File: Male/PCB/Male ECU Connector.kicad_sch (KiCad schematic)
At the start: 5 parts, among them J1 ANALYZER, J2 ECU, J3 DJetECUEdgeConnector, K1 G5V-1-DC5

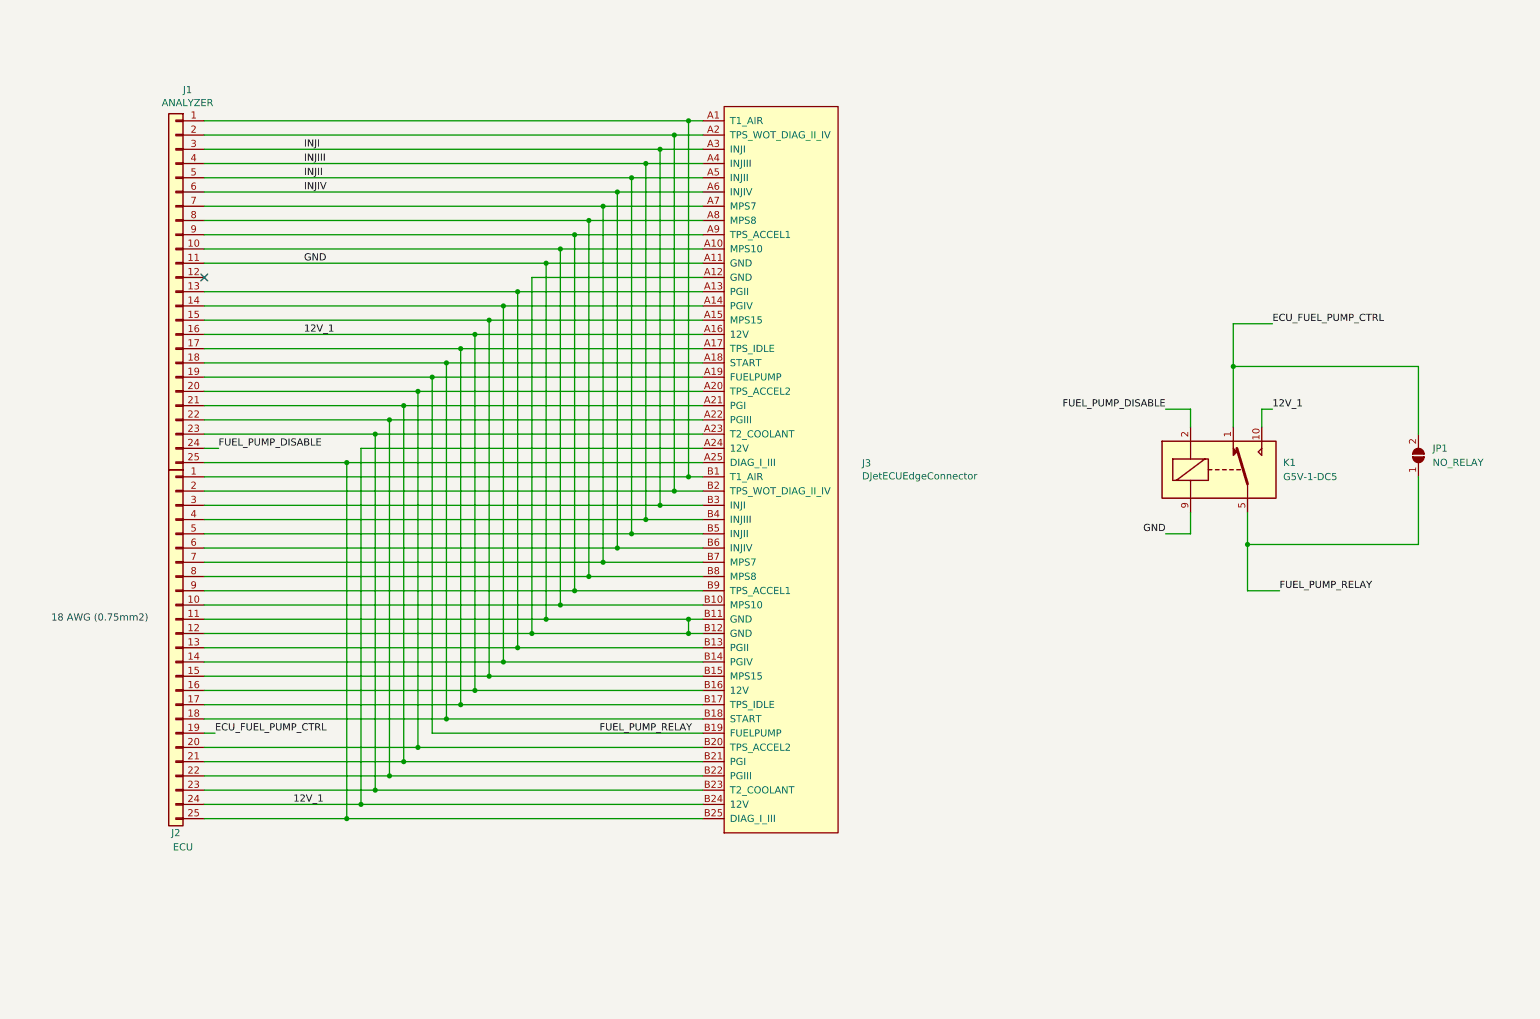
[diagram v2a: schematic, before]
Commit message: Laid out PCB fpr male connector.
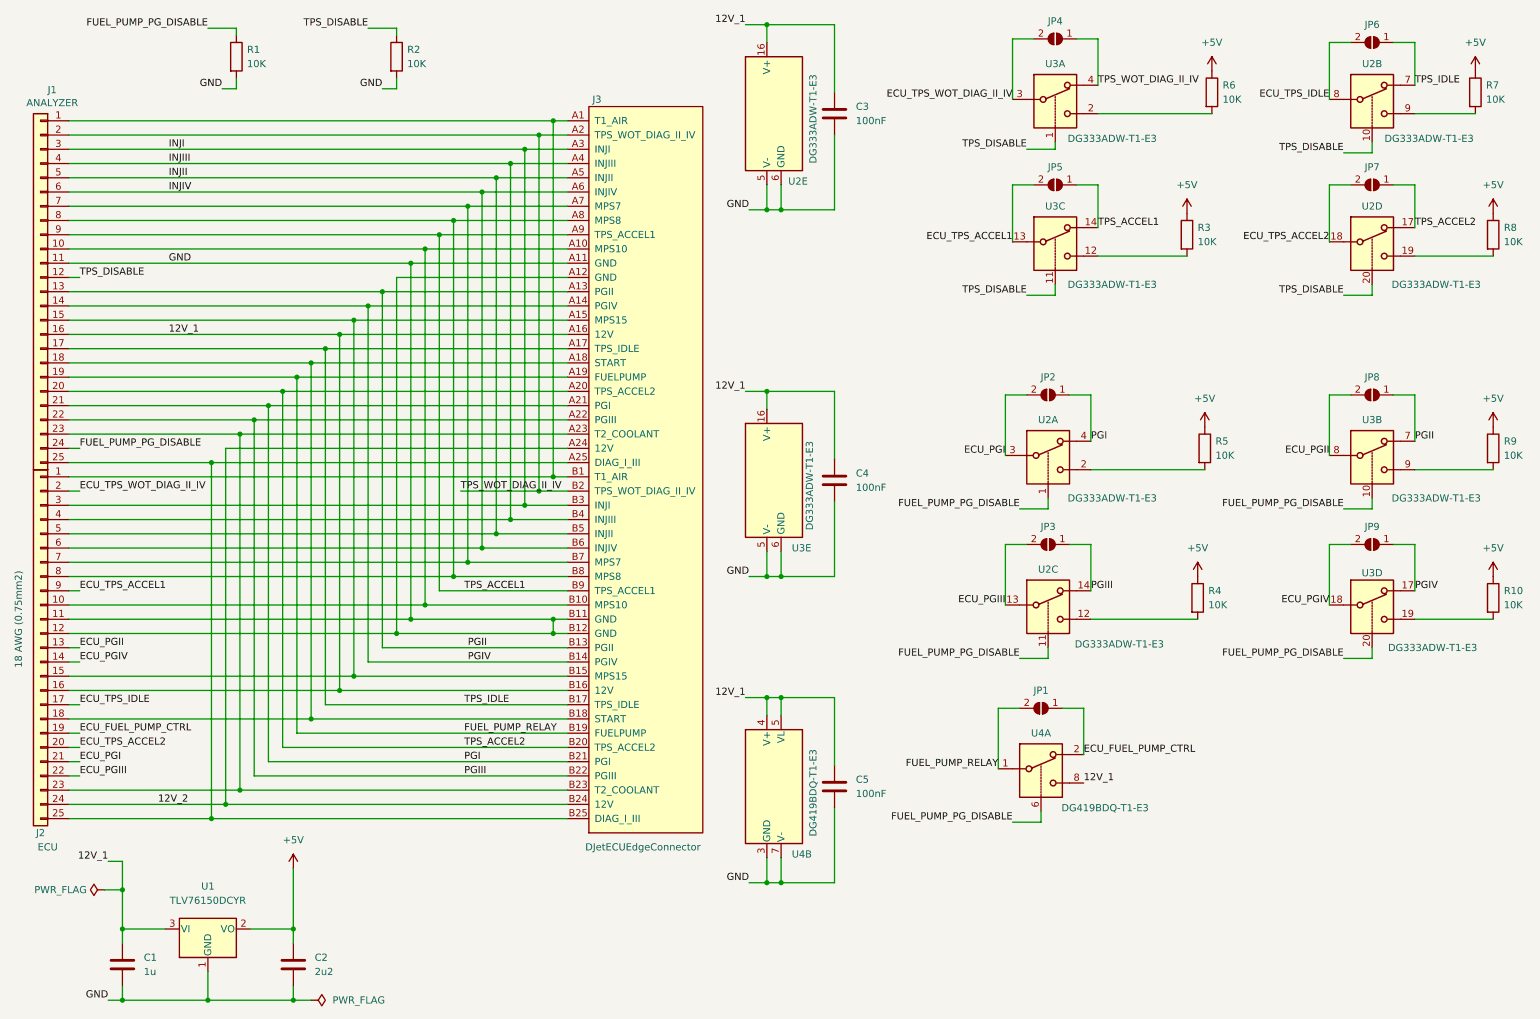
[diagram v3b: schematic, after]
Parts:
- removed K1: G5V-1-DC5, Relay_THT:Relay_SPDT_Omron_G5V-1, symbol Relay:G5V-1
- added C1: 1u, Capacitor_SMD:C_0603_1608Metric, symbol Device:C
- added C2: 2u2, Capacitor_SMD:C_0603_1608Metric, symbol Device:C
- added C3, C4, C5: 100nF, Capacitor_SMD:C_0603_1608Metric, symbol Device:C
- added JP2, JP3, JP4, JP5, JP6, JP7, JP8, JP9: NO_ANALYZER, Jumper:SolderJumper-2_P1.3mm_Open_TrianglePad1.0x1.5mm, symbol Jumper:SolderJumper_2_Open
- added R1, R10, R2, R3, R4, R5, R6, R7, R8, R9: 10K, Resistor_SMD:R_0603_1608Metric, symbol Device:R
- added U1: TLV76150DCYR, Package_TO_SOT_SMD:SOT-223-3_TabPin2, symbol Regulator_Linear:LM1117-5.0
- added U2, U3: DG333ADW-T1-E3, Package_SO:SOIC-20W_7.5x12.8mm_P1.27mm, symbol Analog_Switch:MAX333A
- added U4: DG419BDQ-T1-E3, Package_SO:MSOP-8_3x3mm_P0.65mm, symbol Analog_Switch:DG419xY
- JP1: value NO_RELAY -> NO_ANALYZER
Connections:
- net 12V_1: now also C1.1, C3.1, C4.1, C5.1, U1.3 (VI), U2.16 (V+), U3.16 (V+), U4.4 (V+), U4.5 (VL), U4.8; no longer J2.24 (Pin_24), J3.A24 (12V), J3.B24 (12V)
- net ECU_FUEL_PUMP_CTRL: now also JP1.1 (A), U4.2; no longer JP1.2 (B)
- net FUEL_PUMP_RELAY: now also JP1.2 (B), U4.1; no longer JP1.1 (A)
- net GND: now also C1.2, C2.2, C3.2, C4.2, C5.2, R1.2, R2.2, U1.1 (GND), U2.5 (V-), U2.6 (GND), U3.5 (V-), U3.6 (GND), U4.3 (GND), U4.7 (V-)
- net TPS_DISABLE: now reaches J1.12 (Pin_12)
- net TPS_DISABLE: now also R2.1, U2.10, U2.20, U3.1, U3.11
- net PGII: now reaches J1.13 (Pin_13), J3.A13 (PGII), J3.B13 (PGII)
- net PGII: now also JP8.1 (A), U3.7; no longer J2.13 (Pin_13)
- net PGIV: now reaches J1.14 (Pin_14), J3.A14 (PGIV), J3.B14 (PGIV)
- net PGIV: now also JP9.1 (A), U3.17; no longer J2.14 (Pin_14)
- net TPS_IDLE: now reaches J1.17 (Pin_17), J3.A17 (TPS_IDLE), J3.B17 (TPS_IDLE)
- net TPS_IDLE: now also JP6.1 (A), U2.7; no longer J2.17 (Pin_17)
- net TPS_WOT_DIAG_II_IV: now reaches J1.2 (Pin_2), J3.A2 (TPS_WOT_DIAG_II_IV), J3.B2 (TPS_WOT_DIAG_II_IV)
- net TPS_WOT_DIAG_II_IV: now also JP4.1 (A), U3.4; no longer J2.2 (Pin_2)
- net TPS_ACCEL2: now reaches J1.20 (Pin_20), J3.A20 (TPS_ACCEL2), J3.B20 (TPS_ACCEL2)
- net TPS_ACCEL2: now also JP7.1 (A), U2.17; no longer J2.20 (Pin_20)
- net PGI: now reaches J1.21 (Pin_21), J3.A21 (PGI), J3.B21 (PGI)
- net PGI: now also JP2.1 (A), U2.4; no longer J2.21 (Pin_21)
- net PGIII: now reaches J1.22 (Pin_22), J3.A22 (PGIII), J3.B22 (PGIII)
- net PGIII: now also JP3.1 (A), U2.14; no longer J2.22 (Pin_22)
- net TPS_ACCEL1: now reaches J1.9 (Pin_9), J3.A9 (TPS_ACCEL1), J3.B9 (TPS_ACCEL1)
- net TPS_ACCEL1: now also JP5.1 (A), U3.14; no longer J2.9 (Pin_9)
- net FUEL_PUMP_DISABLE renamed FUEL_PUMP_PG_DISABLE
- net FUEL_PUMP_PG_DISABLE: now also R1.1, U2.1, U2.11, U3.10, U3.20, U4.6
- new net: R5.2, U2.2
- new net: R3.2, U3.12
- new net: R10.2, U3.19
- new net: R9.2, U3.9
- new net: R6.2, U3.2
- new net: R8.2, U2.19
- new net: R4.2, U2.12
- new net: R7.2, U2.9
- new net +5V: C2.1, R10.1, R3.1, R4.1, R5.1, R6.1, R7.1, R8.1, R9.1, U1.2 (VO)
- new net 12V_2: J2.24 (Pin_24), J3.A24 (12V), J3.B24 (12V)
- new net ECU_PGI: J2.21 (Pin_21), JP2.2 (B), U2.3
- new net ECU_PGII: J2.13 (Pin_13), JP8.2 (B), U3.8
- new net ECU_PGIII: J2.22 (Pin_22), JP3.2 (B), U2.13
- new net ECU_PGIV: J2.14 (Pin_14), JP9.2 (B), U3.18
- new net ECU_TPS_ACCEL1: J2.9 (Pin_9), JP5.2 (B), U3.13
- new net ECU_TPS_ACCEL2: J2.20 (Pin_20), JP7.2 (B), U2.18
- new net ECU_TPS_IDLE: J2.17 (Pin_17), JP6.2 (B), U2.8
- new net ECU_TPS_WOT_DIAG_II_IV: J2.2 (Pin_2), JP4.2 (B), U3.3
- no-connect marks 1 -> 0
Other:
- moved on the sheet: J1, J2, J3

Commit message: Completed PCB design for male connector.
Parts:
- added FID1, FID2, FID3: Fiducial, Fiducial:Fiducial_0.5mm_Mask1.5mm, symbol Mechanical:Fiducial
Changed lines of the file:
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@@
   (title_block
     (title "Male ECU Connector for D-Jetronic")
-    (date "2023-11-04")
+    (date "2023-11-11")
     (rev "V1.1")
     (company "djetronic.org")
@@
     (pin "2")
   )
+  (symbol (lib_id "Mechanical:Fiducial") (at 132.715 189.23 0) (unit 1)
+    (in_bom yes) (on_board yes) (fields_autoplaced)
+    (property "Reference" "FID1" (id 0) (at 135.89 187.9599 0)
+      (effects (font (size 1.27 1.27)) (justify left))
+    )
+    (property "Value" "Fiducial" (id 1) (at 135.89 190.4999 0)
+      (effects (font (size 1.27 1.27)) (justify left))
+    )
+    (property "Footprint" "Fiducial:Fiducial_0.5mm_Mask1.5mm" (id 2) (at 132.715 189.23 0)
+      (effects (font (size 1.27 1.27)) hide)
+    )
+    (property "Datasheet" "~" (id 3) (at 132.715 189.23 0)
+      (effects (font (size 1.27 1.27)) hide)
+    )
+  )
+  (symbol (lib_id "Mechanical:Fiducial") (at 146.685 189.23 0) (unit 1)
+    (in_bom yes) (on_board yes) (fields_autoplaced)
+    (property "Reference" "FID2" (id 0) (at 149.86 187.9599 0)
+      (effects (font (size 1.27 1.27)) (justify left))
+    )
+    (property "Value" "Fiducial" (id 1) (at 149.86 190.4999 0)
+      (effects (font (size 1.27 1.27)) (justify left))
+    )
+    (property "Footprint" "Fiducial:Fiducial_0.5mm_Mask1.5mm" (id 2) (at 146.685 189.23 0)
+      (effects (font (size 1.27 1.27)) hide)
+    )
+    (property "Datasheet" "~" (id 3) (at 146.685 189.23 0)
+      (effects (font (size 1.27 1.27)) hide)
+    )
+  )
   (symbol (lib_id "Analog_Switch:MAX333A") (at 199.39 118.11 0) (unit 3)
     (in_bom yes) (on_board yes)
@@
     (pin "2")
   )
+  (symbol (lib_id "Mechanical:Fiducial") (at 160.655 189.23 0) (unit 1)
+    (in_bom yes) (on_board yes) (fields_autoplaced)
+    (property "Reference" "FID3" (id 0) (at 163.83 187.9599 0)
+      (effects (font (size 1.27 1.27)) (justify left))
+    )
+    (property "Value" "Fiducial" (id 1) (at 163.83 190.4999 0)
+      (effects (font (size 1.27 1.27)) (justify left))
+    )
+    (property "Footprint" "Fiducial:Fiducial_0.5mm_Mask1.5mm" (id 2) (at 160.655 189.23 0)
+      (effects (font (size 1.27 1.27)) hide)
+    )
+    (property "Datasheet" "~" (id 3) (at 160.655 189.23 0)
+      (effects (font (size 1.27 1.27)) hide)
+    )
+  )
   (symbol (lib_id "Analog_Switch:DG419xY") (at 149.225 153.035 0) (unit 2)
     (in_bom yes) (on_board yes)
@@
       (reference "C5") (unit 1) (value "100nF") (footprint "Capacitor_SMD:C_0603_1608Metric")
     )
+    (path "/73393203-f71d-4a6b-8390-f6ea05706212"
+      (reference "FID1") (unit 1) (value "Fiducial") (footprint "Fiducial:Fiducial_0.5mm_Mask1.5mm")
+    )
+    (path "/74859361-2ce1-4972-8cb8-18c26e371fc6"
+      (reference "FID2") (unit 1) (value "Fiducial") (footprint "Fiducial:Fiducial_0.5mm_Mask1.5mm")
+    )
+    (path "/e8e90ee4-9ff7-4d10-88ac-c06ee51b9160"
+      (reference "FID3") (unit 1) (value "Fiducial") (footprint "Fiducial:Fiducial_0.5mm_Mask1.5mm")
+    )
     (path "/00000000-0000-0000-0000-000063a3ff2d"

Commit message: Changed analyzer connector to DB25.
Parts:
- J1: footprint Connector_PinHeader_2.54mm:PinHeader_1x25_P2.54mm_Vertical -> Connector_Dsub:DSUB-25_Female_Horizontal_P2.77x2.84mm_EdgePinOffset7.70mm_Housed_MountingHolesOffset9.12mm; manf# (none) -> A-DF 25 A/KG-T2S
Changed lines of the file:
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@@
   (title_block
     (title "Male ECU Connector for D-Jetronic")
-    (date "2023-11-11")
+    (date "2023-11-19")
     (rev "V1.1")
     (company "djetronic.org")
@@
     (property "Reference" "J1" (id 0) (at 21.7678 28.7782 0))
     (property "Value" "ANALYZER" (id 1) (at 21.7678 31.0896 0))
-    (property "Footprint" "Connector_PinHeader_2.54mm:PinHeader_1x25_P2.54mm_Vertical" (id 2) (at 19.685 64.77 0)
+    (property "Footprint" "Connector_Dsub:DSUB-25_Female_Horizontal_P2.77x2.84mm_EdgePinOffset7.70mm_Housed_MountingHolesOffset9.12mm" (id 2) (at 19.685 64.77 0)
       (effects (font (size 1.27 1.27)) hide)
     )
     (property "Datasheet" "~" (id 3) (at 19.685 64.77 0)
+      (effects (font (size 1.27 1.27)) hide)
+    )
+    (property "manf#" "A-DF 25 A/KG-T2S" (id 4) (at 19.685 64.77 0)
       (effects (font (size 1.27 1.27)) hide)
     )
@@
     )
     (path "/00000000-0000-0000-0000-000063a3ff2d"
-      (reference "J1") (unit 1) (value "ANALYZER") (footprint "Connector_PinHeader_2.54mm:PinHeader_1x25_P2.54mm_Vertical")
+      (reference "J1") (unit 1) (value "ANALYZER") (footprint "Connector_Dsub:DSUB-25_Female_Horizontal_P2.77x2.84mm_EdgePinOffset7.70mm_Housed_MountingHolesOffset9.12mm")
     )
     (path "/00000000-0000-0000-0000-000063a4c84d"
